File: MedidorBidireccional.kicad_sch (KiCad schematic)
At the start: 28 parts, among them J1 ADC conector, J2 Pickit, J3 JP, U1 RN4870-I_RM140, U2 47L04-E_ST, U3 25AA320A-I_ST, U4 PIC24FJ128GA310-I_PT

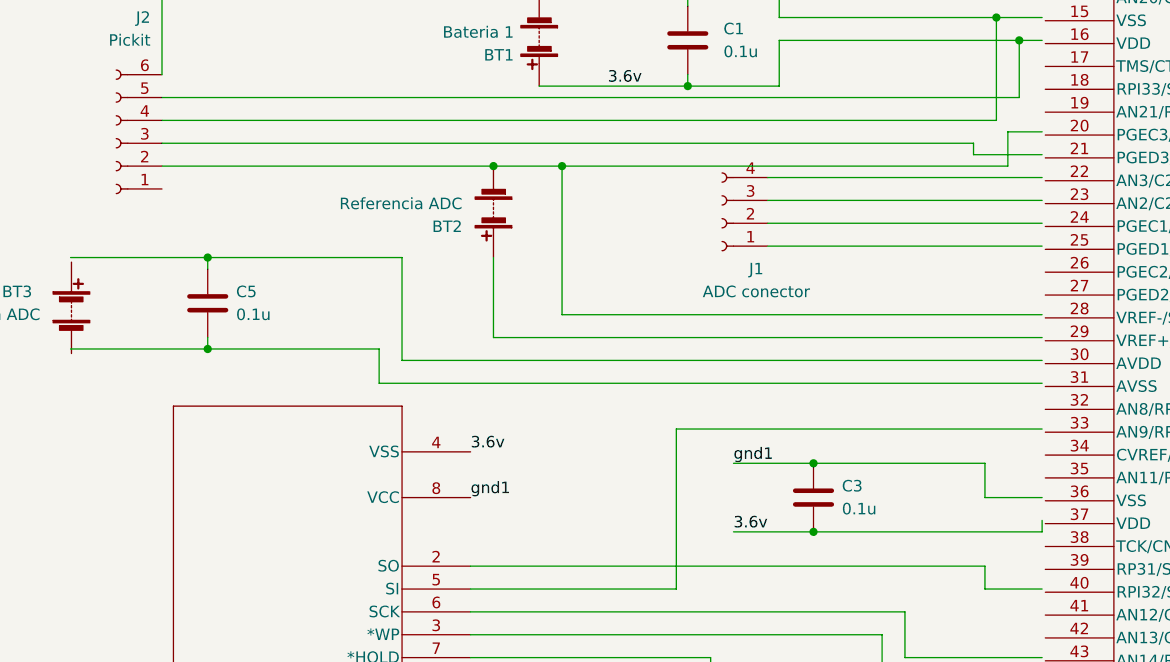
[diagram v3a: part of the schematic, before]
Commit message: correcion de diagrama
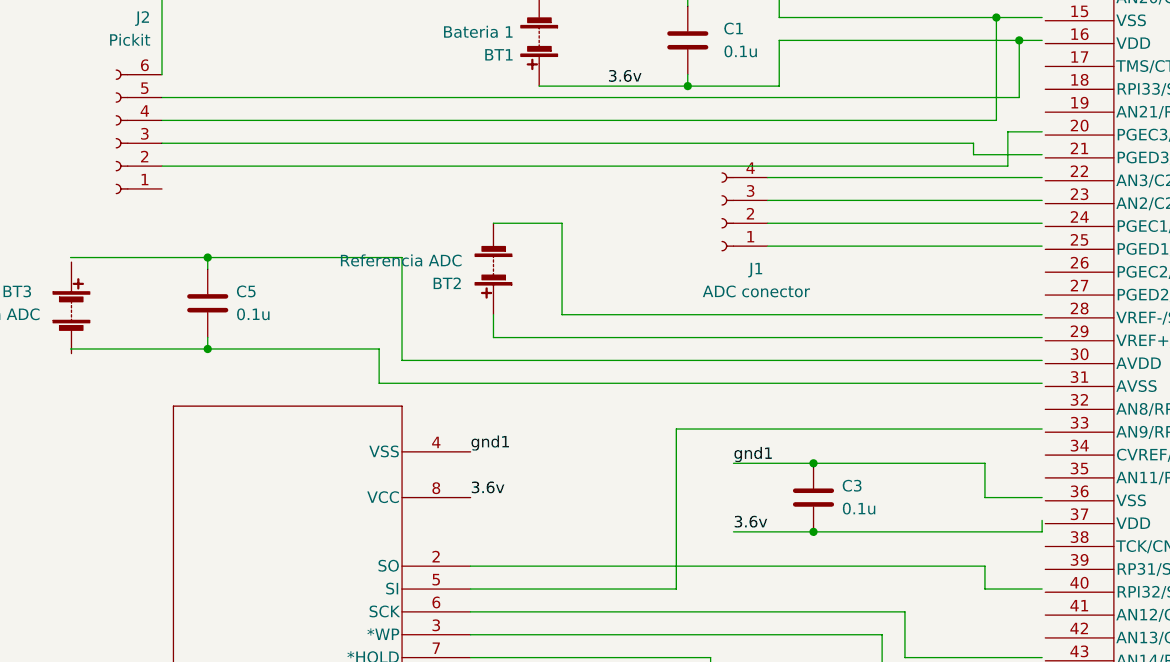
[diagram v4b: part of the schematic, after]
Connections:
- net 3.6v: now also U3.8 (VCC); no longer U3.4 (VSS)
- net gnd1: now also U3.4 (VSS); no longer U3.8 (VCC)
- net at J2.2 (Pin_2): no longer BT2.2 (-)
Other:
- moved on the sheet: BT2
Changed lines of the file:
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@@
   (junction (at 35.56 118.11) (diameter 0) (color 0 0 0 0)
   )
-  (junction (at 162.56 185.42) (diameter 0) (color 0 0 0 0)
-  )
   (junction (at 35.56 115.57) (diameter 0) (color 0 0 0 0)
   )
@@
   )
   (junction (at 198.12 226.06) (diameter 0) (color 0 0 0 0)
-  )
-  (junction (at 170.18 185.42) (diameter 0) (color 0 0 0 0)
   )
   (junction (at 299.72 111.76) (diameter 0) (color 0 0 0 0)
@@
     (stroke (width 0) (type default) (color 0 0 0 0))
   )
-  (wire (pts (xy 125.73 185.42) (xy 162.56 185.42))
-    (stroke (width 0) (type default) (color 0 0 0 0))
-  )
   (wire (pts (xy 193.04 194.31) (xy 223.52 194.31))
     (stroke (width 0) (type default) (color 0 0 0 0))
@@
     (stroke (width 0) (type default) (color 0 0 0 0))
   )
+  (wire (pts (xy 170.18 201.93) (xy 170.18 191.77))
+    (stroke (width 0) (type default) (color 0 0 0 0))
+  )
   (wire (pts (xy 96.52 156.21) (xy 223.52 156.21))
     (stroke (width 0) (type default) (color 0 0 0 0))
@@
     (stroke (width 0) (type default) (color 0 0 0 0))
   )
-  (wire (pts (xy 162.56 195.58) (xy 162.56 204.47))
+  (wire (pts (xy 162.56 201.93) (xy 162.56 204.47))
     (stroke (width 0) (type default) (color 0 0 0 0))
   )
@@
     (stroke (width 0) (type default) (color 0 0 0 0))
   )
-  (wire (pts (xy 170.18 185.42) (xy 170.18 201.93))
-    (stroke (width 0) (type default) (color 0 0 0 0))
-  )
   (wire (pts (xy 189.23 218.44) (xy 198.12 218.44))
     (stroke (width 0) (type default) (color 0 0 0 0))
@@
     (stroke (width 0) (type default) (color 0 0 0 0))
   )
+  (wire (pts (xy 170.18 191.77) (xy 162.56 191.77))
+    (stroke (width 0) (type default) (color 0 0 0 0))
+  )
   (wire (pts (xy 505.46 101.6) (xy 505.46 110.49))
     (stroke (width 0) (type default) (color 0 0 0 0))
@@
     (stroke (width 0) (type default) (color 0 0 0 0))
   )
-  (wire (pts (xy 162.56 185.42) (xy 170.18 185.42))
+  (wire (pts (xy 125.73 185.42) (xy 219.71 185.42))
     (stroke (width 0) (type default) (color 0 0 0 0))
   )
@@
     (stroke (width 0) (type default) (color 0 0 0 0))
   )
-  (wire (pts (xy 170.18 185.42) (xy 219.71 185.42))
-    (stroke (width 0) (type default) (color 0 0 0 0))
-  )
   (wire (pts (xy 125.73 175.26) (xy 125.73 162.56))
     (stroke (width 0) (type default) (color 0 0 0 0))
@@
     (effects (font (size 1.27 1.27)) (justify left bottom))
   )
-  (label "3.6v" (at 160.02 217.17 0)
+  (label "3.6v" (at 160.02 222.25 0)
     (effects (font (size 1.27 1.27)) (justify left bottom))
   )
@@
     (effects (font (size 1.27 1.27)) (justify left bottom))
   )
-  (label "gnd1" (at 160.02 222.25 0)
+  (label "gnd1" (at 160.02 217.17 0)
     (effects (font (size 1.27 1.27)) (justify left bottom))
   )
@@
     (pin "8")
   )
-  (symbol (lib_id "Device:Battery") (at 162.56 190.5 180) (unit 1)
+  (symbol (lib_id "Device:Battery") (at 162.56 196.85 180) (unit 1)
     (in_bom yes) (on_board yes) (fields_autoplaced)
-    (property "Reference" "BT2" (id 0) (at 159.1056 192.1511 0)
-      (effects (font (size 1.27 1.27)) (justify left))
-    )
-    (property "Value" "Referencia ADC" (id 1) (at 159.1056 189.6111 0)
-      (effects (font (size 1.27 1.27)) (justify left))
-    )
-    (property "Footprint" "" (id 2) (at 162.56 192.024 90)
-      (effects (font (size 1.27 1.27)) hide)
-    )
-    (property "Datasheet" "~" (id 3) (at 162.56 192.024 90)
-      (effects (font (size 1.27 1.27)) hide)
-    )
+    (property "Reference" "BT2" (id 0) (at 159.1056 198.5011 0)
+      (effects (font (size 1.27 1.27)) (justify left))
+    )
+    (property "Value" "Referencia ADC" (id 1) (at 159.1056 195.9611 0)
+      (effects (font (size 1.27 1.27)) (justify left))
+    )
+    (property "Footprint" "" (id 2) (at 162.56 198.374 90)
+      (effects (font (size 1.27 1.27)) hide)
+    )
+    (property "Datasheet" "~" (id 3) (at 162.56 198.374 90)
+      (effects (font (size 1.27 1.27)) hide)
+    )
